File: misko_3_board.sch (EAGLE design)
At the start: 179 parts, among them IC1 ATMEGA1281-16AU, IC10 ORG1510-MK4, IC11 TPS3808G33DBVT, IC12 LTC4425, IC13 RN-42, IC14 ADXL345, IC15 74HCT1G32, IC16 FM25W256-SOIC, IC17 MICROSD_SPI_MODE, IC18 FH12-30S-0.5SH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

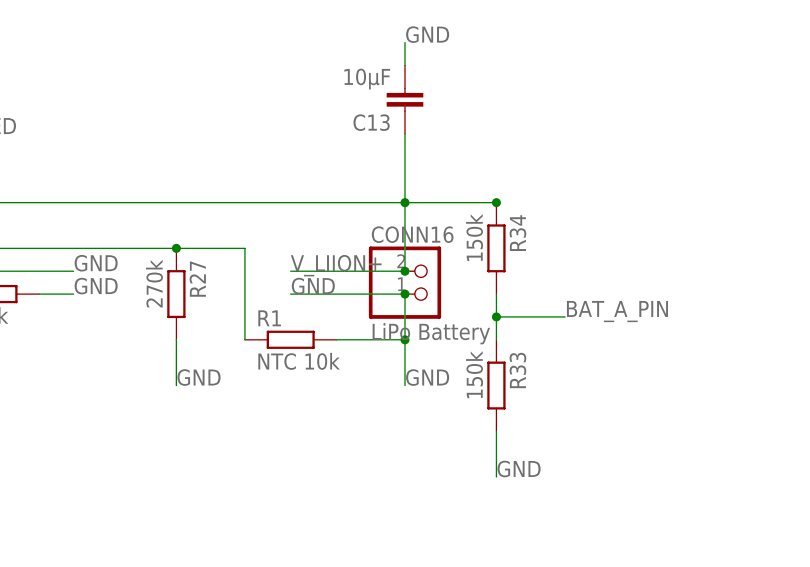
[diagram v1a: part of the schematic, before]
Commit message: - changed orientation of JST-PH battery connector (--> polarity)
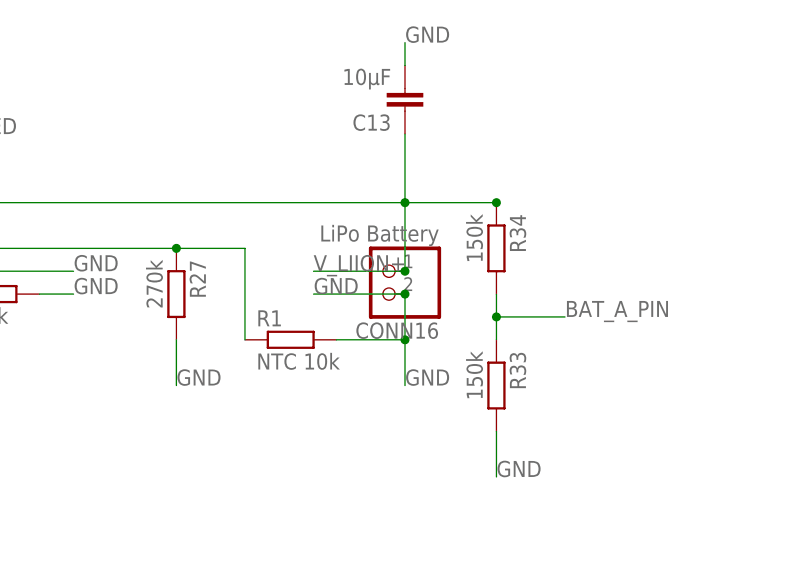
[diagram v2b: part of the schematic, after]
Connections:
- net GND: now also CONN16.1; no longer CONN16.2
- net V_LIION+: now also CONN16.2; no longer CONN16.1
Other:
- moved on the sheet: CONN16
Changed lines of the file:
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@@
 <instance part="S2" gate="G$1" x="40.64" y="467.36" rot="R90"/>
 <instance part="C14" gate="G$1" x="182.88" y="596.9" rot="R180"/>
-<instance part="CONN16" gate="G$1" x="320.04" y="510.54"/>
+<instance part="CONN16" gate="G$1" x="314.96" y="513.08" rot="R180"/>
 <instance part="IC10" gate="G$1" x="48.26" y="38.1"/>
 <instance part="R36" gate="G$1" x="35.56" y="68.58" rot="R90"/>
@@
 <pinref part="R1" gate="G$1" pin="2"/>
 <wire x1="309.88" y1="505.46" x2="317.5" y2="505.46" width="0.1524" layer="91"/>
-<pinref part="CONN16" gate="G$1" pin="2"/>
-<wire x1="317.5" y1="510.54" x2="317.5" y2="505.46" width="0.1524" layer="91"/>
+<label x="317.5" y="500.38" size="1.778" layer="95" ratio="9"/>
+<pinref part="CONN16" gate="G$1" pin="1"/>
+<wire x1="317.5" y1="505.46" x2="317.5" y2="510.54" width="0.1524" layer="91"/>
 <junction x="317.5" y="505.46"/>
-<wire x1="317.5" y1="510.54" x2="304.8" y2="510.54" width="0.1524" layer="91"/>
+<wire x1="317.5" y1="510.54" x2="307.34" y2="510.54" width="0.1524" layer="91"/>
 <junction x="317.5" y="510.54"/>
-<label x="304.8" y="510.54" size="1.778" layer="95"/>
-<label x="317.5" y="500.38" size="1.778" layer="95" ratio="9"/>
+<label x="307.34" y="510.54" size="1.778" layer="95"/>
 </segment>
 <segment>
@@
 <wire x1="317.5" y1="528.32" x2="317.5" y2="520.7" width="0.1524" layer="91"/>
 <junction x="327.66" y="520.7"/>
-<pinref part="CONN16" gate="G$1" pin="1"/>
+<pinref part="CONN16" gate="G$1" pin="2"/>
 <wire x1="317.5" y1="513.08" x2="317.5" y2="520.7" width="0.1524" layer="91"/>
-<wire x1="317.5" y1="513.08" x2="304.8" y2="513.08" width="0.1524" layer="91"/>
+<wire x1="317.5" y1="513.08" x2="307.34" y2="513.08" width="0.1524" layer="91"/>
 <junction x="317.5" y="513.08"/>
-<label x="304.8" y="513.08" size="1.778" layer="95"/>
+<label x="307.34" y="513.08" size="1.778" layer="95"/>
 </segment>
 </net>

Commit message: - bill of materials in csv format - unified voltage divider resistors - corrected capacitor value 100nF -> 0.1µF
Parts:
- C10: value 100nF -> 0.1µF
- R25, R35: value 200k -> 150k
- R37, R38: value 100k -> 150k
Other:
- moved on the sheet: C44, C45, C46, C47, C49, D2
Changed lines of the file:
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@@
 <part name="R34" library="rcl" deviceset="R-EU_" device="R0805" value="150k"/>
 <part name="GND1" library="supply1" deviceset="GND" device=""/>
-<part name="R25" library="rcl" deviceset="R-EU_" device="R0805" value="200k"/>
-<part name="R35" library="rcl" deviceset="R-EU_" device="R0805" value="200k"/>
+<part name="R25" library="rcl" deviceset="R-EU_" device="R0805" value="150k"/>
+<part name="R35" library="rcl" deviceset="R-EU_" device="R0805" value="150k"/>
 <part name="S2" library="smd-special" deviceset="SWS001" device="" value="POWER_SWITCH"/>
 <part name="C14" library="resistor" deviceset="C-EU" device="C0805" value="0.1µF"/>
@@
 <part name="IC13" library="EN42-I Bluetooth Module" deviceset="RN-42" device=""/>
 <part name="IC12" library="LTC4425 Supercap Charger" deviceset="LTC4425" device=""/>
-<part name="R37" library="resistor" deviceset="R-EU_" device="R0805" value="100k"/>
-<part name="R38" library="resistor" deviceset="R-EU_" device="R0805" value="100k"/>
+<part name="R37" library="resistor" deviceset="R-EU_" device="R0805" value="150k"/>
+<part name="R38" library="resistor" deviceset="R-EU_" device="R0805" value="150k"/>
 <part name="R39" library="resistor" deviceset="R-EU_" device="R0805" value="1k"/>
 <part name="R40" library="resistor" deviceset="R-EU_" device="R0805" value="10k"/>
@@
 <part name="CONN14" library="MX500075-1517 USB Mini-B straight socket" deviceset="MX500075-1517USB_MINI-B" device=""/>
 <part name="L3" library="DJNR6045-100S Power Inductor" deviceset="DJNR6045-100-S" device=""/>
-<part name="C10" library="resistor" deviceset="C-EU" device="C0805" value="100nF"/>
+<part name="C10" library="resistor" deviceset="C-EU" device="C0805" value="0.1µF"/>
 <part name="S3" library="micro joystick" deviceset="MICROJOYSTICK" device=""/>
 <part name="TP11" library="testpad" deviceset="PTR1" device="TP14R" value="VGPS"/>
@@
 <instance part="FI1" gate="G$1" x="396.24" y="525.78"/>
 <instance part="FI2" gate="G$1" x="421.64" y="525.78"/>
-<instance part="C49" gate="G$1" x="447.04" y="472.44"/>
-<instance part="C44" gate="G$1" x="459.74" y="472.44"/>
-<instance part="C45" gate="G$1" x="472.44" y="472.44"/>
-<instance part="C46" gate="G$1" x="485.14" y="472.44"/>
-<instance part="C47" gate="G$1" x="497.84" y="472.44"/>
-<instance part="D2" gate="G$1" x="436.88" y="474.98" rot="R270"/>
+<instance part="C49" gate="G$1" x="274.32" y="472.44"/>
+<instance part="C44" gate="G$1" x="287.02" y="472.44"/>
+<instance part="C45" gate="G$1" x="299.72" y="472.44"/>
+<instance part="C46" gate="G$1" x="312.42" y="472.44"/>
+<instance part="C47" gate="G$1" x="325.12" y="472.44"/>
+<instance part="D2" gate="G$1" x="264.16" y="474.98" rot="R270"/>
 </instances>
 <busses>
@@
 </segment>
 <segment>
-<wire x1="447.04" y1="467.36" x2="459.74" y2="467.36" width="0.1524" layer="91"/>
-<wire x1="459.74" y1="467.36" x2="472.44" y2="467.36" width="0.1524" layer="91"/>
-<wire x1="472.44" y1="467.36" x2="485.14" y2="467.36" width="0.1524" layer="91"/>
-<wire x1="485.14" y1="467.36" x2="497.84" y2="467.36" width="0.1524" layer="91"/>
-<wire x1="447.04" y1="467.36" x2="424.18" y2="467.36" width="0.1524" layer="91"/>
-<label x="424.18" y="467.36" size="1.778" layer="95"/>
+<wire x1="274.32" y1="467.36" x2="287.02" y2="467.36" width="0.1524" layer="91"/>
+<wire x1="287.02" y1="467.36" x2="299.72" y2="467.36" width="0.1524" layer="91"/>
+<wire x1="299.72" y1="467.36" x2="312.42" y2="467.36" width="0.1524" layer="91"/>
+<wire x1="312.42" y1="467.36" x2="325.12" y2="467.36" width="0.1524" layer="91"/>
+<wire x1="274.32" y1="467.36" x2="251.46" y2="467.36" width="0.1524" layer="91"/>
+<label x="251.46" y="467.36" size="1.778" layer="95"/>
 <pinref part="C49" gate="G$1" pin="-"/>
-<junction x="447.04" y="467.36"/>
+<junction x="274.32" y="467.36"/>
 <pinref part="C44" gate="G$1" pin="-"/>
-<junction x="459.74" y="467.36"/>
+<junction x="287.02" y="467.36"/>
 <pinref part="C45" gate="G$1" pin="-"/>
-<junction x="472.44" y="467.36"/>
+<junction x="299.72" y="467.36"/>
 <pinref part="C46" gate="G$1" pin="-"/>
-<junction x="485.14" y="467.36"/>
+<junction x="312.42" y="467.36"/>
 <pinref part="C47" gate="G$1" pin="-"/>
 </segment>
@@
 <segment>
 <pinref part="D2" gate="G$1" pin="C"/>
-<wire x1="434.34" y1="474.98" x2="424.18" y2="474.98" width="0.1524" layer="91"/>
-<label x="424.18" y="474.98" size="1.778" layer="95"/>
+<wire x1="261.62" y1="474.98" x2="251.46" y2="474.98" width="0.1524" layer="91"/>
+<label x="251.46" y="474.98" size="1.778" layer="95"/>
 </segment>
 </net>
@@
 <net name="N$6" class="0">
 <segment>
-<wire x1="447.04" y1="474.98" x2="459.74" y2="474.98" width="0.1524" layer="91"/>
+<wire x1="274.32" y1="474.98" x2="287.02" y2="474.98" width="0.1524" layer="91"/>
 <pinref part="C49" gate="G$1" pin="+"/>
 <pinref part="C44" gate="G$1" pin="+"/>
-<wire x1="459.74" y1="474.98" x2="472.44" y2="474.98" width="0.1524" layer="91"/>
-<junction x="459.74" y="474.98"/>
+<wire x1="287.02" y1="474.98" x2="299.72" y2="474.98" width="0.1524" layer="91"/>
+<junction x="287.02" y="474.98"/>
 <pinref part="C45" gate="G$1" pin="+"/>
-<wire x1="472.44" y1="474.98" x2="485.14" y2="474.98" width="0.1524" layer="91"/>
-<junction x="472.44" y="474.98"/>
+<wire x1="299.72" y1="474.98" x2="312.42" y2="474.98" width="0.1524" layer="91"/>
+<junction x="299.72" y="474.98"/>
 <pinref part="C46" gate="G$1" pin="+"/>
-<wire x1="485.14" y1="474.98" x2="497.84" y2="474.98" width="0.1524" layer="91"/>
-<junction x="485.14" y="474.98"/>
+<wire x1="312.42" y1="474.98" x2="325.12" y2="474.98" width="0.1524" layer="91"/>
+<junction x="312.42" y="474.98"/>
 <pinref part="C47" gate="G$1" pin="+"/>
 <pinref part="D2" gate="G$1" pin="A"/>
-<wire x1="439.42" y1="474.98" x2="447.04" y2="474.98" width="0.1524" layer="91"/>
-<junction x="447.04" y="474.98"/>
+<wire x1="266.7" y1="474.98" x2="274.32" y2="474.98" width="0.1524" layer="91"/>
+<junction x="274.32" y="474.98"/>
 </segment>
 </net>

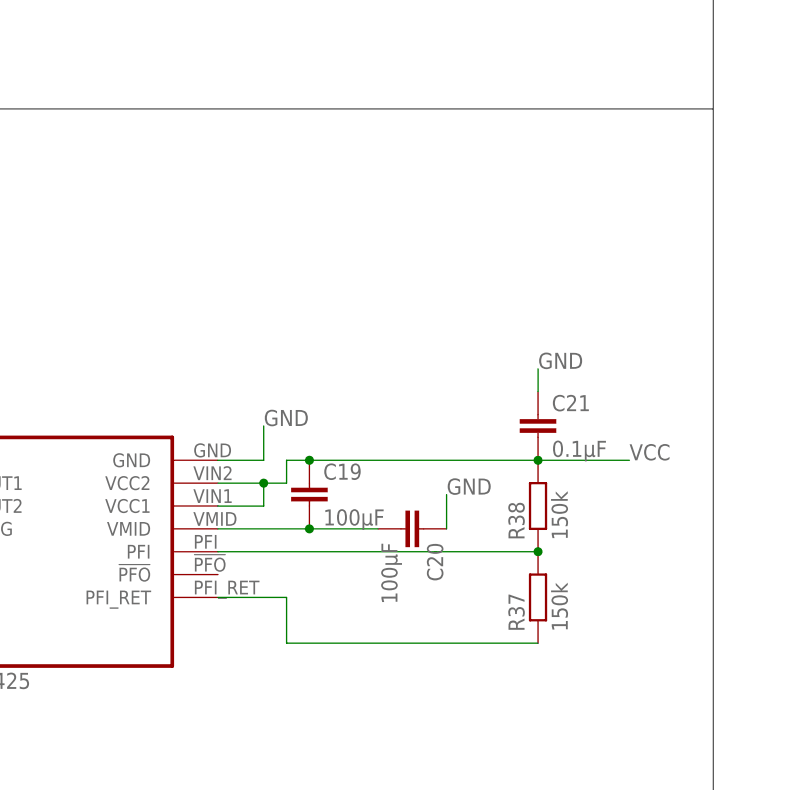
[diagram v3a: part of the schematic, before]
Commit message: - replaced LTC4425's Vmid capacitor divider by resistors -
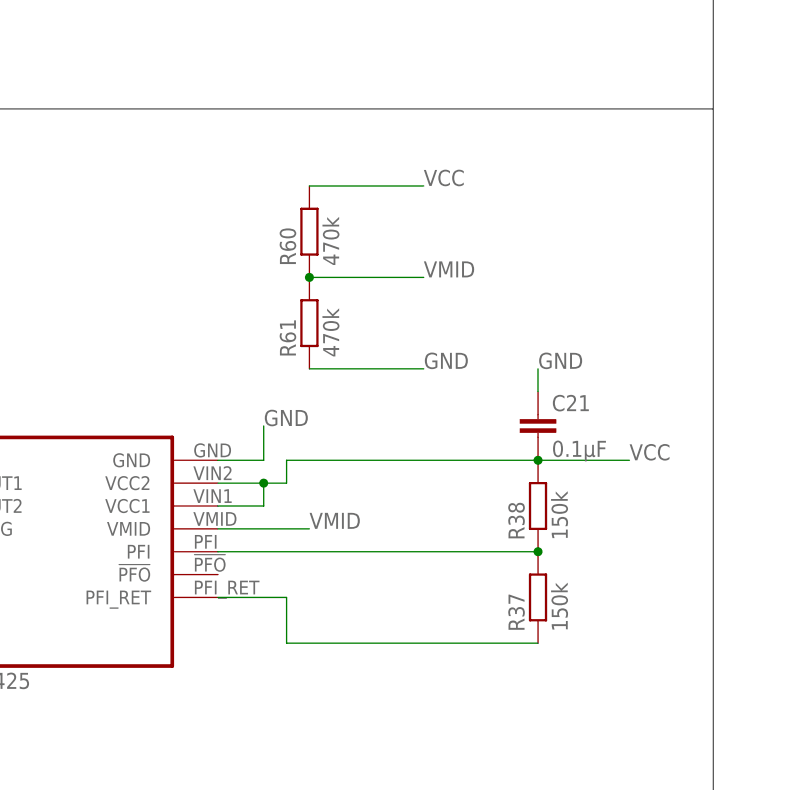
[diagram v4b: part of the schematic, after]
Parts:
- removed C19, C20: 100µF, rcl:C-EUC0805
- added R60, R61: 470k, resistor:R-EU_R0805
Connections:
- net GND: now also R61.1; no longer C20.1
- net VCC: now also R60.2; no longer C19.1
- net VMID: now also R60.1, R61.2; no longer C19.2, C20.2
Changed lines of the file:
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@@
 <part name="R39" library="resistor" deviceset="R-EU_" device="R0805" value="1k"/>
 <part name="R40" library="resistor" deviceset="R-EU_" device="R0805" value="10k"/>
-<part name="C19" library="rcl" deviceset="C-EU" device="C0805" value="100µF"/>
-<part name="C20" library="rcl" deviceset="C-EU" device="C0805" value="100µF"/>
 <part name="C21" library="rcl" deviceset="C-EU" device="C0805" value="0.1µF"/>
 <part name="IC16" library="FM25W256 FERAM" deviceset="FM25W256" device="-SOIC"/>
@@
 <part name="C47" library="rcl" deviceset="CPOL-EU" device="E22-10AXIAL" value="1000µF"/>
 <part name="D2" library="eagle-ltspice" deviceset="SCHOTTKY-DIODE" device="F126Z12"/>
+<part name="R60" library="resistor" deviceset="R-EU_" device="R0805" value="470k"/>
+<part name="R61" library="resistor" deviceset="R-EU_" device="R0805" value="470k"/>
 </parts>
 <sheets>
@@
 <instance part="R39" gate="G$1" x="266.7" y="48.26"/>
 <instance part="R40" gate="G$1" x="269.24" y="55.88"/>
-<instance part="C19" gate="G$1" x="325.12" y="60.96"/>
-<instance part="C20" gate="G$1" x="337.82" y="55.88" rot="R270"/>
 <instance part="C21" gate="G$1" x="350.52" y="68.58"/>
 <instance part="IC16" gate="G$1" x="198.12" y="-132.08"/>
@@
 <instance part="C47" gate="G$1" x="325.12" y="472.44"/>
 <instance part="D2" gate="G$1" x="264.16" y="474.98" rot="R270"/>
+<instance part="R60" gate="G$1" x="325.12" y="88.9" rot="R90"/>
+<instance part="R61" gate="G$1" x="325.12" y="78.74" rot="R90"/>
 </instances>
 <busses>
@@
 <pinref part="IC12" gate="G$1" pin="VCC1"/>
 <wire x1="320.04" y1="58.42" x2="314.96" y2="58.42" width="0.1524" layer="91"/>
-<pinref part="C19" gate="G$1" pin="1"/>
-<wire x1="325.12" y1="63.5" x2="322.58" y2="63.5" width="0.1524" layer="91"/>
 <wire x1="322.58" y1="63.5" x2="322.58" y2="60.96" width="0.1524" layer="91"/>
 <wire x1="322.58" y1="60.96" x2="320.04" y2="60.96" width="0.1524" layer="91"/>
 <junction x="320.04" y="60.96"/>
-<wire x1="325.12" y1="63.5" x2="350.52" y2="63.5" width="0.1524" layer="91"/>
-<junction x="325.12" y="63.5"/>
+<wire x1="322.58" y1="63.5" x2="350.52" y2="63.5" width="0.1524" layer="91"/>
 <pinref part="R38" gate="G$1" pin="2"/>
 <pinref part="C21" gate="G$1" pin="2"/>
@@
 <label x="284.48" y="830.58" size="1.778" layer="95" ratio="9"/>
 </segment>
+<segment>
+<pinref part="R60" gate="G$1" pin="2"/>
+<wire x1="325.12" y1="93.98" x2="337.82" y2="93.98" width="0.1524" layer="91"/>
+<label x="337.82" y="93.98" size="1.778" layer="95"/>
+</segment>
 </net>
 <net name="GND" class="0">
@@
 </segment>
 <segment>
-<pinref part="C20" gate="G$1" pin="1"/>
-<wire x1="340.36" y1="59.69" x2="340.36" y2="55.88" width="0.1524" layer="91"/>
-<label x="340.36" y="59.69" size="1.778" layer="95" ratio="9"/>
-</segment>
-<segment>
 <pinref part="IC13" gate="G$1" pin="GPIO3"/>
 <wire x1="177.8" y1="-27.94" x2="154.94" y2="-27.94" width="0.1524" layer="91"/>
@@
 <label x="284.48" y="840.74" size="1.778" layer="95" ratio="9"/>
 </segment>
+<segment>
+<pinref part="R61" gate="G$1" pin="1"/>
+<wire x1="325.12" y1="73.66" x2="337.82" y2="73.66" width="0.1524" layer="91"/>
+<label x="337.82" y="73.66" size="1.778" layer="95"/>
+</segment>
 </net>
 <net name="5V0" class="1">
@@
 <net name="VMID" class="2">
 <segment>
-<pinref part="C19" gate="G$1" pin="2"/>
 <pinref part="IC12" gate="G$1" pin="VMID"/>
 <wire x1="325.12" y1="55.88" x2="314.96" y2="55.88" width="0.1524" layer="91"/>
-<junction x="325.12" y="55.88"/>
-<pinref part="C20" gate="G$1" pin="2"/>
-<wire x1="325.12" y1="55.88" x2="332.74" y2="55.88" width="0.1524" layer="91"/>
+<label x="325.12" y="55.88" size="1.778" layer="95"/>
+</segment>
+<segment>
+<pinref part="R60" gate="G$1" pin="1"/>
+<pinref part="R61" gate="G$1" pin="2"/>
+<wire x1="325.12" y1="83.82" x2="337.82" y2="83.82" width="0.1524" layer="91"/>
+<junction x="325.12" y="83.82"/>
+<label x="337.82" y="83.82" size="1.778" layer="95"/>
 </segment>
 </net>

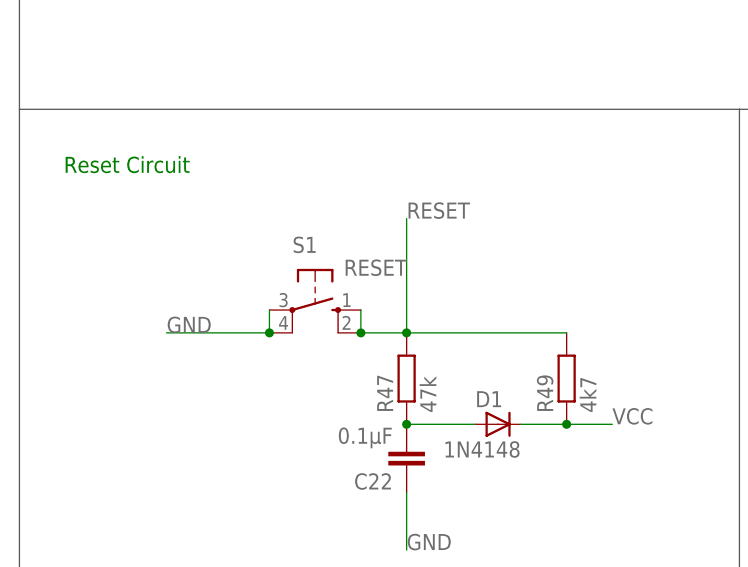
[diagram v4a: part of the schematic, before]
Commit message: - replaced TH reset switch with smaller SMD part
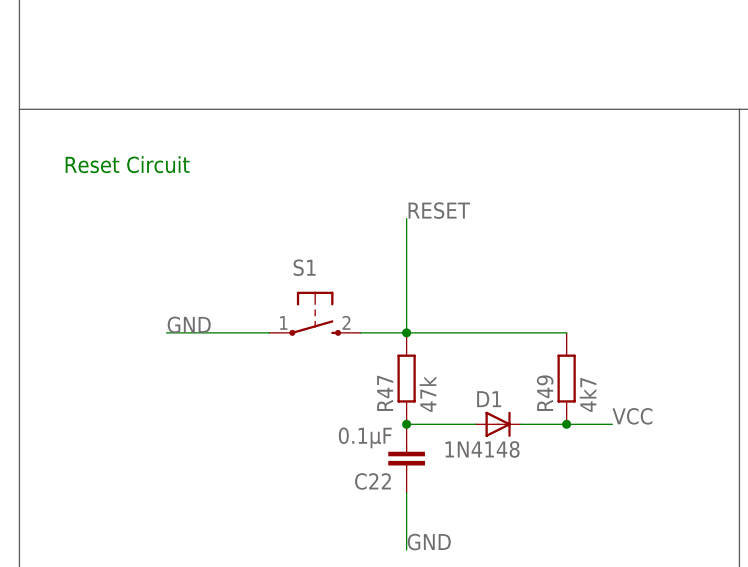
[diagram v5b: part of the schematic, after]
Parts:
- S1: value RESET -> (none); device switch-omron:10-XX -> DTSM-32N-B:DTSM-32N-B
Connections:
- net GND: now also S1.1; no longer S1.P, S1.P1
- net RESET: now also S1.2; no longer S1.S, S1.S1
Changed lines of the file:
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@@
 <part name="R45" library="rcl" deviceset="R-EU_" device="R0805" value="1k"/>
 <part name="R46" library="rcl" deviceset="R-EU_" device="R0805" value="1k"/>
-<part name="S1" library="switch-omron" deviceset="10-XX" device="" value="RESET"/>
 <part name="R47" library="rcl" deviceset="R-EU_" device="R0805" value="47k"/>
 <part name="R49" library="rcl" deviceset="R-EU_" device="R0805" value="4k7"/>
@@
 <part name="R60" library="resistor" deviceset="R-EU_" device="R0805" value="470k"/>
 <part name="R61" library="resistor" deviceset="R-EU_" device="R0805" value="470k"/>
+<part name="S1" library="DTSM-32N-B" deviceset="DTSM-32N-B" device=""/>
 </parts>
 <sheets>
@@
 <instance part="R45" gate="G$1" x="162.56" y="635"/>
 <instance part="R46" gate="G$1" x="162.56" y="645.16"/>
-<instance part="S1" gate="1" x="22.86" y="647.7" rot="R270"/>
 <instance part="R47" gate="G$1" x="33.02" y="640.08" rot="R90"/>
 <instance part="R49" gate="G$1" x="50.8" y="640.08" rot="R90"/>
@@
 <instance part="R60" gate="G$1" x="325.12" y="88.9" rot="R90"/>
 <instance part="R61" gate="G$1" x="325.12" y="78.74" rot="R90"/>
+<instance part="S1" gate="1" x="22.86" y="645.16" rot="R270"/>
 </instances>
 <busses>
@@
 </segment>
 <segment>
-<pinref part="S1" gate="1" pin="P"/>
-<pinref part="S1" gate="1" pin="P1"/>
 <wire x1="6.35" y1="645.16" x2="17.78" y2="645.16" width="0.1524" layer="91"/>
-<wire x1="17.78" y1="647.7" x2="17.78" y2="645.16" width="0.1524" layer="91"/>
-<junction x="17.78" y="645.16"/>
 <label x="6.35" y="645.16" size="1.778" layer="95" ratio="9"/>
+<pinref part="S1" gate="1" pin="1"/>
 </segment>
 <segment>
@@
 </segment>
 <segment>
-<pinref part="S1" gate="1" pin="S"/>
-<pinref part="S1" gate="1" pin="S1"/>
 <pinref part="R47" gate="G$1" pin="2"/>
 <wire x1="27.94" y1="645.16" x2="33.02" y2="645.16" width="0.1524" layer="91"/>
@@
 <wire x1="33.02" y1="645.16" x2="33.02" y2="657.86" width="0.1524" layer="91"/>
 <label x="33.02" y="657.86" size="1.778" layer="95"/>
-<wire x1="27.94" y1="647.7" x2="27.94" y2="645.16" width="0.1524" layer="91"/>
-<junction x="27.94" y="645.16"/>
+<pinref part="S1" gate="1" pin="2"/>
 </segment>
 <segment>
